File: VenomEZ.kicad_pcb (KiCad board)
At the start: 2 copper layers, 72 x 42 mm, 42 parts, among them CN1 HC-XH-5A-G, CN10 HC-XH-2A-G, CN2 HC-PH-8A-G, CN3 HC-XH-8A-G, CN4 HC-XH-8A-G, CN5 HC-XH-2A-G, CN6 HC-PH-7A-G, CN7 HC-XH-2A-G, CN8 HC-XH-2A-G, CN9 HC-XH-2A-G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

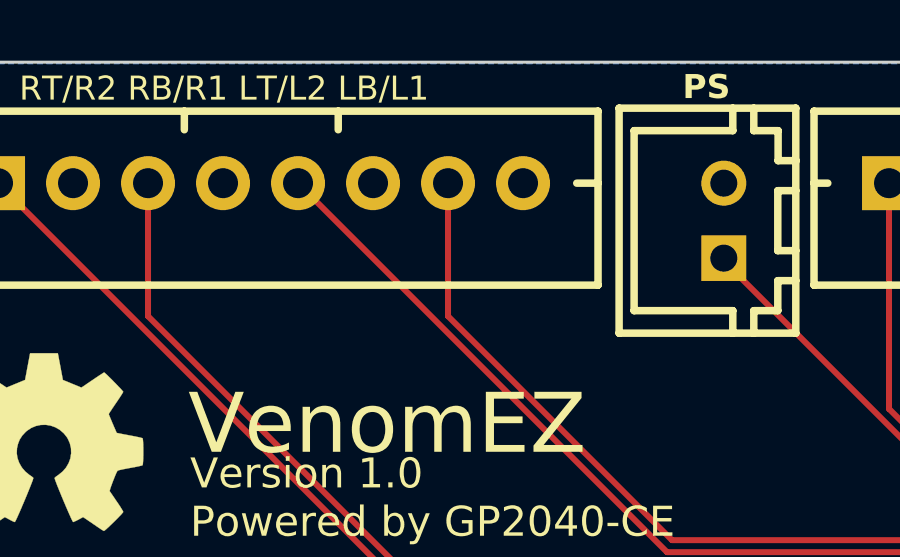
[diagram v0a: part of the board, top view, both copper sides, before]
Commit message: Add hidden "JLCJLCJLCJLC"
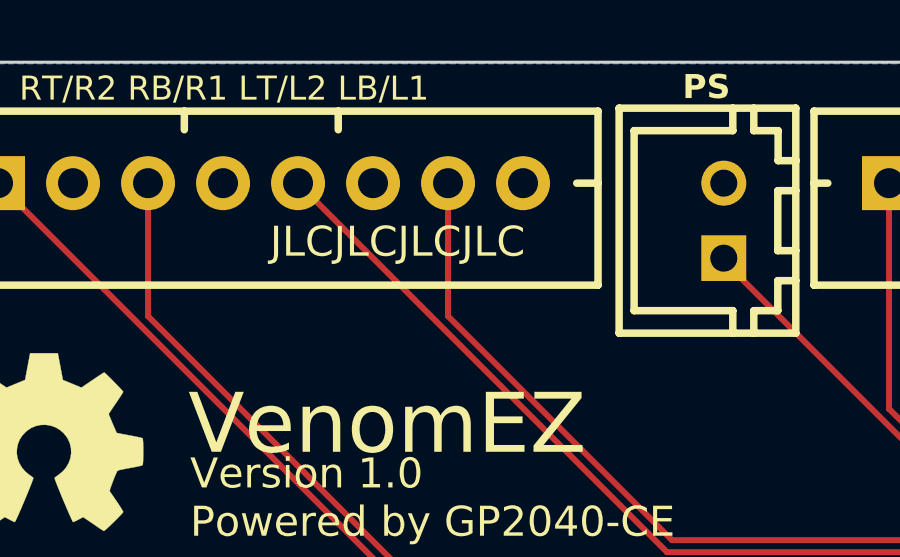
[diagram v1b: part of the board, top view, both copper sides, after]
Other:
- board text added: "JLCJLCJLCJLC"
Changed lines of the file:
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@@
     (effects (font (size 0.8 0.8) (thickness 0.15)) (justify left bottom))
+  )
+  (gr_text "JLCJLCJLCJLC" (at 99.06 81.28) (layer "F.SilkS")
+    (effects (font (size 1 1) (thickness 0.15)) (justify left bottom))
   )
   (gr_text "LED" (at 131.756309 115) (layer "F.SilkS")

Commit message: Update PH connectors to ones JLC stock
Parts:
- CN2: footprint easyeda2kicad:CONN-TH_8P-P2.00_HCTL_HC-PH-8A-X -> easyeda2kicad:CONN-TH_8P-P2.00_PH-8A
- CN6: footprint easyeda2kicad:CONN-TH_7P-P2.00_HCTL_HC-PH-7A-X -> easyeda2kicad:CONN-TH_7P-P2.00_PH-7A
- moved CN2 0.07 mm to (113.0, 111.3)
